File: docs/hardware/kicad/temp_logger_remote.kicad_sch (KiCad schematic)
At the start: 29 parts, among them J1 BP_SOCKET_LEFT, J10 TEMP2_OUT, J2 BP_SOCKET_RIGHT, J3 NRF24_SOCKET, J4 JST-B2B-PH-K-S, J5 JST-B2B-PH-K-S, J6 JST-PHR-2, J7 JST-PHR-2, J8 USB_B_Micro, J9 TEMP1_OUT

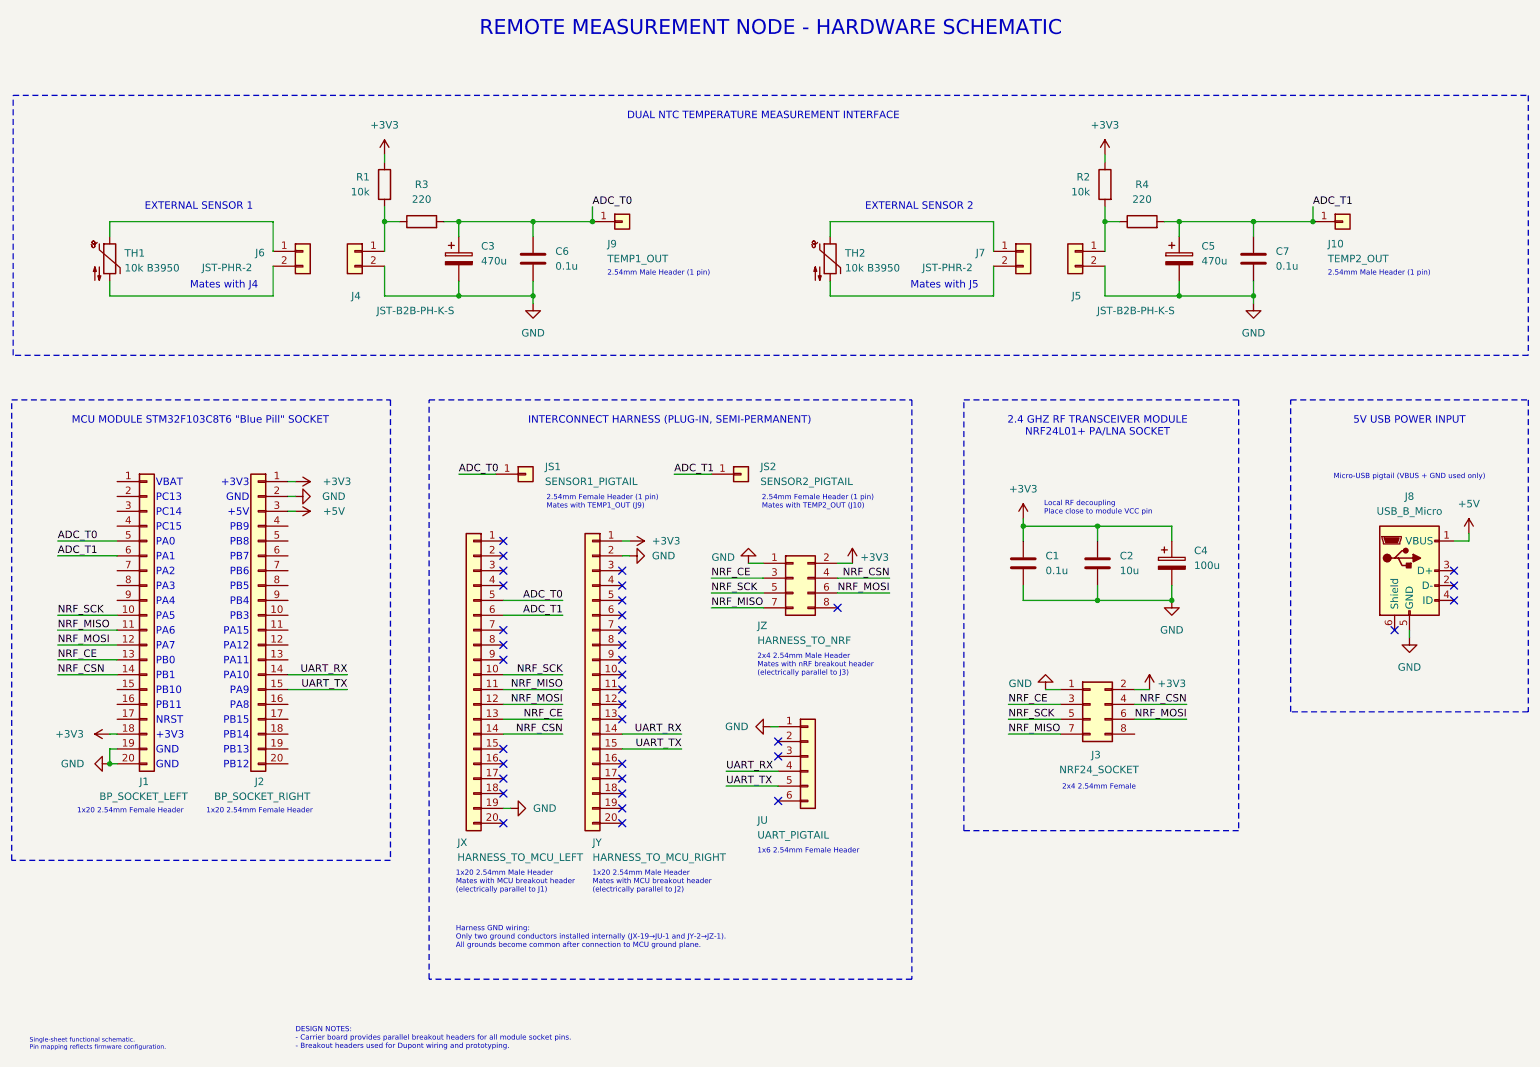
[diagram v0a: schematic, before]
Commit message: Update README: switch to RevB schematic and document ADC filter improvement
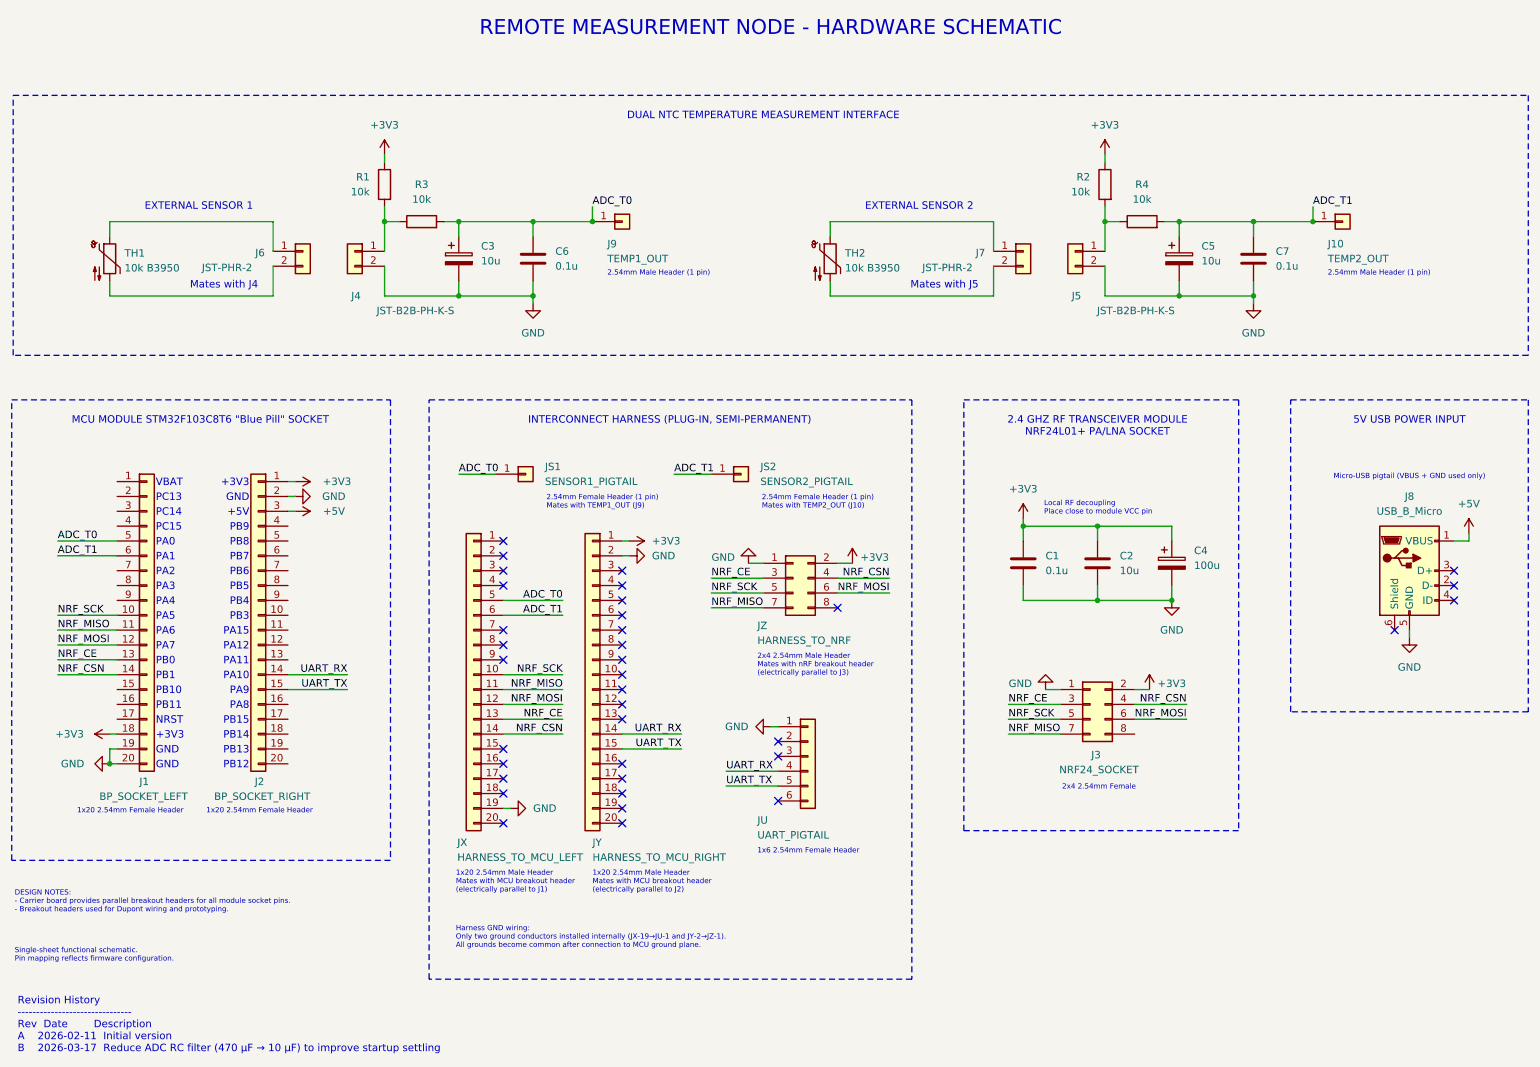
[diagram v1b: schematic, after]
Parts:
- C3, C5: value 470u -> 10u
- R3, R4: value 220 -> 10k
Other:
- note added: "Revision History ------------------------------- Rev Date Description A 2026-02-11 Initial version B 2026-03-17 Reduce ADC RC filter (470 µF → 10 µF) to improve startup settling"
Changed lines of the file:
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@@
 	(title_block
 		(title "STM32 nRF24 Temperature Logger – Remote Node")
-		(date "2026-02-11")
-		(rev "A")
+		(date "2026-03-17")
+		(rev "B")
 		(company "Jani Honkanen")
-		(comment 1 "Remote measurement node – Rev A prototype")
+		(comment 1 "Remote measurement node – Rev B prototype")
 	)
 	(rectangle
@@
 	(text "Single-sheet functional schematic.\nPin mapping reflects firmware configuration."
 		(exclude_from_sim no)
-		(at 21.844 190.246 0)
+		(at 19.304 175.006 0)
 		(effects
 			(font
-				(size 0.762 0.762)
+				(size 0.889 0.889)
 			)
 			(justify left)
@@
 		)
 	)
+	(text "Revision History\n-------------------------------\nRev  Date        Description\nA    2026-02-11  Initial version\nB    2026-03-17  Reduce ADC RC filter (470 µF → 10 µF) to improve startup settling"
+		(exclude_from_sim no)
+		(at 19.812 186.944 0)
+		(effects
+			(font
+				(face "Consolas")
+				(size 1.27 1.27)
+			)
+			(justify left)
+		)
+	)
 	(text "2x4 2.54mm Male Header\nMates with nRF breakout header\n(electrically parallel to J3)\n\n"
 		(exclude_from_sim no)
@@
 	(text "DESIGN NOTES:\n- Carrier board provides parallel breakout headers for all module socket pins.\n- Breakout headers used for Dupont wiring and prototyping."
 		(exclude_from_sim no)
-		(at 67.31 189.23 0)
+		(at 19.304 165.862 0)
 		(effects
 			(font
@@
 			)
 		)
-		(property "Value" "470u"
+		(property "Value" "10u"
 			(at 99.06 56.2609 0)
 			(effects
@@
 			)
 		)
-		(property "Value" "470u"
+		(property "Value" "10u"
 			(at 222.25 56.2609 0)
 			(effects
@@
 			)
 		)
-		(property "Value" "220"
+		(property "Value" "10k"
 			(at 88.9 45.72 90)
 			(effects
@@
 			)
 		)
-		(property "Value" "220"
+		(property "Value" "10k"
 			(at 212.09 45.72 90)
 			(effects
